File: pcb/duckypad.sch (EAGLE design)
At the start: 160 parts, among them IC2 REG1117, SW1 SPST_TACT-EVQQ2, SW2 SPST_TACT-EVQQ2, SW21 EC12E_SW, SW22 EC12E_SW, SW3 324_SW324_SWITCH_FOOT_HOLE, SW4 324_SW324_SWITCH_FOOT_HOLE, U1 USBC_16P, U2 USBC_16P, U3 ESP32-S3FN8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

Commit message: updated pcb files
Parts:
- removed JP3: (no value), adafruit_changed:PINHD-1X1CB
- removed U$3: BUZZ40402, duckypad:BUZZ40402
- added BZ1: BUZZ40402, duckypad:BUZZ40402
- added D22: 1N4148, duckypad:ADAFRUIT_CHANGED_DIODESOD-123
- added Q1: BSS123, transistor-small-signal:BSS123
- renumbered U$19 to U19
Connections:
- net +3V3: now also BZ1.PLUS, D22.C
- net GND: now also Q1.S, R19.1; no longer U$3.MINUS
- net N$37: now also BZ1.MINUS, D22.A, Q1.D; no longer R19.1, U$3.PLUS
- net N$70: now also Q1.G
- net N$73: no longer JP3.1
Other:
- note added: "BSS138"
- moved on the sheet: R19
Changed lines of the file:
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@@
 <drawing>
 <settings>
-<setting alwaysvectorfont="no"/>
+<setting alwaysvectorfont="yes"/>
 <setting keepoldvectorfont="yes"/>
 <setting verticaltext="up"/>
@@
 <part name="C28" library="clock" deviceset="CAP" device="0805" value="100nF"/>
 <part name="GND40" library="supply1" library_urn="urn:adsk.eagle:library:371" deviceset="GND" device=""/>
-<part name="U$19" library="SparkFun-Retired" deviceset="V_REG_TPS61040" device="SMD"/>
+<part name="U19" library="SparkFun-Retired" deviceset="V_REG_TPS61040" device="SMD"/>
 <part name="+3V32" library="supply1" library_urn="urn:adsk.eagle:library:371" deviceset="+3V3" device=""/>
 <part name="GND44" library="supply1" deviceset="GND" device=""/>
@@
 <part name="R17" library="joyAnalog" deviceset="RESISTOR" device="0805-RES" value="5K1"/>
 <part name="GND62" library="supply1" library_urn="urn:adsk.eagle:library:371" deviceset="GND" device=""/>
-<part name="JP3" library="adafruit_changed" deviceset="PINHD-1X1" device="CB"/>
 <part name="D1" library="duckypad" deviceset="ADAFRUIT_CHANGED_DIODE" device="SOD-123" value="1N4148"/>
 <part name="SW4" library="3pos_slide_switch" deviceset="324_SW" device="324_SWITCH_FOOT_HOLE" value="324_SW324_SWITCH_FOOT_HOLE"/>
@@
 <part name="GND65" library="supply1" deviceset="GND" device=""/>
 <part name="JP4" library="SparkFun-Jumpers" deviceset="JUMPER-SMT_2_NO" device="_NO-SILK"/>
-<part name="U$3" library="duckypad" deviceset="BUZZ40402" device=""/>
-<part name="R19" library="joyAnalog" deviceset="RESISTOR" device="0805-RES" value="5K1"/>
+<part name="BZ1" library="duckypad" deviceset="BUZZ40402" device=""/>
 <part name="GND41" library="supply1" deviceset="GND" device=""/>
+<part name="Q1" library="transistor-small-signal" library_urn="urn:adsk.eagle:library:401" deviceset="BSS123" device="" package3d_urn="urn:adsk.eagle:package:28738/2"/>
+<part name="+3V2" library="supply1" library_urn="urn:adsk.eagle:library:371" deviceset="+3V3" device=""/>
+<part name="D22" library="duckypad" deviceset="ADAFRUIT_CHANGED_DIODE" device="SOD-123" value="1N4148"/>
+<part name="R19" library="joyAnalog" deviceset="RESISTOR" device="0805-RES" value="5K1"/>
+<part name="GND67" library="supply1" deviceset="GND" device=""/>
 </parts>
 <sheets>
@@
 <plain>
 <text x="297.18" y="-63.5" size="1.778" layer="94">40MHz!!!</text>
+<text x="63.5" y="-264.16" size="1.778" layer="94">BSS138</text>
 </plain>
 <instances>
@@
 <attribute name="VALUE" x="505.46" y="-35.56" size="1.778" layer="96"/>
 </instance>
-<instance part="U$19" gate="G$1" x="190.5" y="-284.48" smashed="yes">
+<instance part="U19" gate="G$1" x="190.5" y="-284.48" smashed="yes">
 <attribute name="NAME" x="185.42" y="-274.32" size="1.778" layer="95" rot="MR180"/>
 <attribute name="VALUE" x="185.42" y="-294.64" size="1.778" layer="96"/>
@@
 <attribute name="VALUE" x="373.38" y="-297.18" size="1.778" layer="96"/>
 </instance>
-<instance part="JP3" gate="G$1" x="317.5" y="-71.12" smashed="yes" rot="R180">
-<attribute name="NAME" x="323.85" y="-74.295" size="1.778" layer="95" rot="R180"/>
-<attribute name="VALUE" x="323.85" y="-66.04" size="1.778" layer="96" rot="R180"/>
-</instance>
 <instance part="D1" gate="G$1" x="210.82" y="-251.46" smashed="yes">
 <attribute name="NAME" x="208.28" y="-248.92" size="1.27" layer="95"/>
@@
 <attribute name="NAME" x="340.36" y="-7.62" size="1.778" layer="95" font="vector" rot="R90"/>
 </instance>
-<instance part="U$3" gate="G$1" x="93.98" y="-220.98" smashed="yes" rot="MR0"/>
-<instance part="R19" gate="G$1" x="119.38" y="-220.98" smashed="yes" rot="MR180">
-<attribute name="NAME" x="118.11" y="-217.3986" size="1.778" layer="95" rot="MR180"/>
-<attribute name="VALUE" x="118.11" y="-215.138" size="1.778" layer="96" rot="MR180"/>
+<instance part="BZ1" gate="G$1" x="76.2" y="-228.6" smashed="yes" rot="MR270"/>
+<instance part="GND41" gate="1" x="76.2" y="-271.78" smashed="yes" rot="MR0">
+<attribute name="VALUE" x="78.74" y="-274.32" size="1.778" layer="96" rot="MR0"/>
+</instance>
+<instance part="Q1" gate="G$1" x="76.2" y="-256.54" smashed="yes" rot="MR0">
+<attribute name="NAME" x="73.66" y="-256.54" size="1.778" layer="95" rot="MR0"/>
+<attribute name="VALUE" x="73.66" y="-259.08" size="1.778" layer="96" rot="MR0"/>
+</instance>
+<instance part="+3V2" gate="G$1" x="76.2" y="-200.66" smashed="yes" rot="MR0">
+<attribute name="VALUE" x="78.74" y="-205.74" size="1.778" layer="96" rot="MR90"/>
+</instance>
+<instance part="D22" gate="G$1" x="60.96" y="-228.6" smashed="yes" rot="R90">
+<attribute name="NAME" x="58.42" y="-231.14" size="1.27" layer="95" rot="R90"/>
+<attribute name="VALUE" x="64.77" y="-231.14" size="1.27" layer="96" rot="R90"/>
+</instance>
+<instance part="R19" gate="G$1" x="91.44" y="-264.16" smashed="yes" rot="MR90">
+<attribute name="NAME" x="87.8586" y="-265.43" size="1.778" layer="95" rot="MR90"/>
+<attribute name="VALUE" x="85.598" y="-265.43" size="1.778" layer="96" rot="MR90"/>
 </instance>
-<instance part="GND41" gate="1" x="71.12" y="-223.52" smashed="yes" rot="MR0">
-<attribute name="VALUE" x="73.66" y="-226.06" size="1.778" layer="96" rot="MR0"/>
+<instance part="GND67" gate="1" x="91.44" y="-271.78" smashed="yes" rot="MR0">
+<attribute name="VALUE" x="93.98" y="-274.32" size="1.778" layer="96" rot="MR0"/>
 </instance>
 </instances>
@@
 </segment>
 <segment>
-<pinref part="U$19" gate="G$1" pin="GND"/>
+<pinref part="U19" gate="G$1" pin="GND"/>
 <pinref part="GND45" gate="1" pin="GND"/>
 <wire x1="203.2" y1="-284.48" x2="205.74" y2="-284.48" width="0.1524" layer="91"/>
@@
 </segment>
 <segment>
+<pinref part="Q1" gate="G$1" pin="S"/>
 <pinref part="GND41" gate="1" pin="GND"/>
-<pinref part="U$3" gate="G$1" pin="MINUS"/>
-<wire x1="71.12" y1="-220.98" x2="78.74" y2="-220.98" width="0.1524" layer="91"/>
+<wire x1="76.2" y1="-269.24" x2="76.2" y2="-261.62" width="0.1524" layer="91"/>
+</segment>
+<segment>
+<pinref part="R19" gate="G$1" pin="1"/>
+<pinref part="GND67" gate="1" pin="GND"/>
 </segment>
 </net>
@@
 <wire x1="160.02" y1="-266.7" x2="172.72" y2="-266.7" width="0.1524" layer="91"/>
 <junction x="160.02" y="-266.7"/>
-<pinref part="U$19" gate="G$1" pin="VIN"/>
+<pinref part="U19" gate="G$1" pin="VIN"/>
 <wire x1="172.72" y1="-266.7" x2="182.88" y2="-266.7" width="0.1524" layer="91"/>
 <wire x1="180.34" y1="-279.4" x2="172.72" y2="-279.4" width="0.1524" layer="91"/>
 <wire x1="172.72" y1="-279.4" x2="172.72" y2="-266.7" width="0.1524" layer="91"/>
 <junction x="172.72" y="-266.7"/>
-<pinref part="U$19" gate="G$1" pin="EN"/>
+<pinref part="U19" gate="G$1" pin="EN"/>
 <wire x1="180.34" y1="-289.56" x2="172.72" y2="-289.56" width="0.1524" layer="91"/>
 <wire x1="172.72" y1="-289.56" x2="172.72" y2="-279.4" width="0.1524" layer="91"/>
@@
 <wire x1="147.32" y1="-208.28" x2="124.46" y2="-208.28" width="0.1524" layer="91"/>
 </segment>
+<segment>
+<pinref part="+3V2" gate="G$1" pin="+3V3"/>
+<pinref part="BZ1" gate="G$1" pin="PLUS"/>
+<wire x1="76.2" y1="-203.2" x2="76.2" y2="-213.36" width="0.1524" layer="91"/>
+<wire x1="76.2" y1="-213.36" x2="60.96" y2="-213.36" width="0.1524" layer="91"/>
+<wire x1="60.96" y1="-213.36" x2="60.96" y2="-226.06" width="0.1524" layer="91"/>
+<junction x="76.2" y="-213.36"/>
+<pinref part="D22" gate="G$1" pin="C"/>
+</segment>
 </net>
 <net name="USB_DP" class="0">
@@
 <segment>
 <wire x1="195.58" y1="-266.7" x2="205.74" y2="-266.7" width="0.1524" layer="91"/>
-<pinref part="U$19" gate="G$1" pin="SW"/>
+<pinref part="U19" gate="G$1" pin="SW"/>
 <wire x1="203.2" y1="-279.4" x2="205.74" y2="-279.4" width="0.1524" layer="91"/>
 <wire x1="205.74" y1="-279.4" x2="205.74" y2="-266.7" width="0.1524" layer="91"/>
@@
 <net name="N$39" class="0">
 <segment>
-<pinref part="U$19" gate="G$1" pin="FB"/>
+<pinref part="U19" gate="G$1" pin="FB"/>
 <wire x1="203.2" y1="-289.56" x2="208.28" y2="-289.56" width="0.1524" layer="91"/>
 <wire x1="208.28" y1="-289.56" x2="208.28" y2="-284.48" width="0.1524" layer="91"/>
@@
 <wire x1="373.38" y1="-220.98" x2="124.46" y2="-220.98" width="0.1524" layer="91"/>
 <pinref part="SH1" gate="G$1" pin="8"/>
-<pinref part="R19" gate="G$1" pin="2"/>
+<pinref part="Q1" gate="G$1" pin="G"/>
+<wire x1="81.28" y1="-259.08" x2="91.44" y2="-259.08" width="0.1524" layer="91"/>
+<wire x1="91.44" y1="-259.08" x2="99.06" y2="-259.08" width="0.1524" layer="91"/>
+<wire x1="124.46" y1="-220.98" x2="99.06" y2="-220.98" width="0.1524" layer="91"/>
+<wire x1="99.06" y1="-220.98" x2="99.06" y2="-259.08" width="0.1524" layer="91"/>
 <junction x="124.46" y="-220.98"/>
+<pinref part="R19" gate="G$1" pin="2"/>
+<junction x="91.44" y="-259.08"/>
 </segment>
 </net>
@@
 <wire x1="347.98" y1="-71.12" x2="335.28" y2="-71.12" width="0.1524" layer="91"/>
 <wire x1="335.28" y1="-71.12" x2="335.28" y2="-226.06" width="0.1524" layer="91"/>
-<pinref part="JP3" gate="G$1" pin="1"/>
-<wire x1="335.28" y1="-71.12" x2="320.04" y2="-71.12" width="0.1524" layer="91"/>
-<junction x="335.28" y="-71.12"/>
 <wire x1="335.28" y1="-226.06" x2="124.46" y2="-226.06" width="0.1524" layer="91"/>
 <pinref part="SH1" gate="G$1" pin="10"/>
@@
 <net name="N$37" class="0">
 <segment>
-<pinref part="U$3" gate="G$1" pin="PLUS"/>
-<pinref part="R19" gate="G$1" pin="1"/>
-<wire x1="109.22" y1="-220.98" x2="114.3" y2="-220.98" width="0.1524" layer="91"/>
+<pinref part="BZ1" gate="G$1" pin="MINUS"/>
+<pinref part="Q1" gate="G$1" pin="D"/>
+<wire x1="76.2" y1="-243.84" x2="76.2" y2="-251.46" width="0.1524" layer="91"/>
+<wire x1="76.2" y1="-243.84" x2="60.96" y2="-243.84" width="0.1524" layer="91"/>
+<wire x1="60.96" y1="-243.84" x2="60.96" y2="-231.14" width="0.1524" layer="91"/>
+<junction x="76.2" y="-243.84"/>
+<pinref part="D22" gate="G$1" pin="A"/>
 </segment>
 </net>

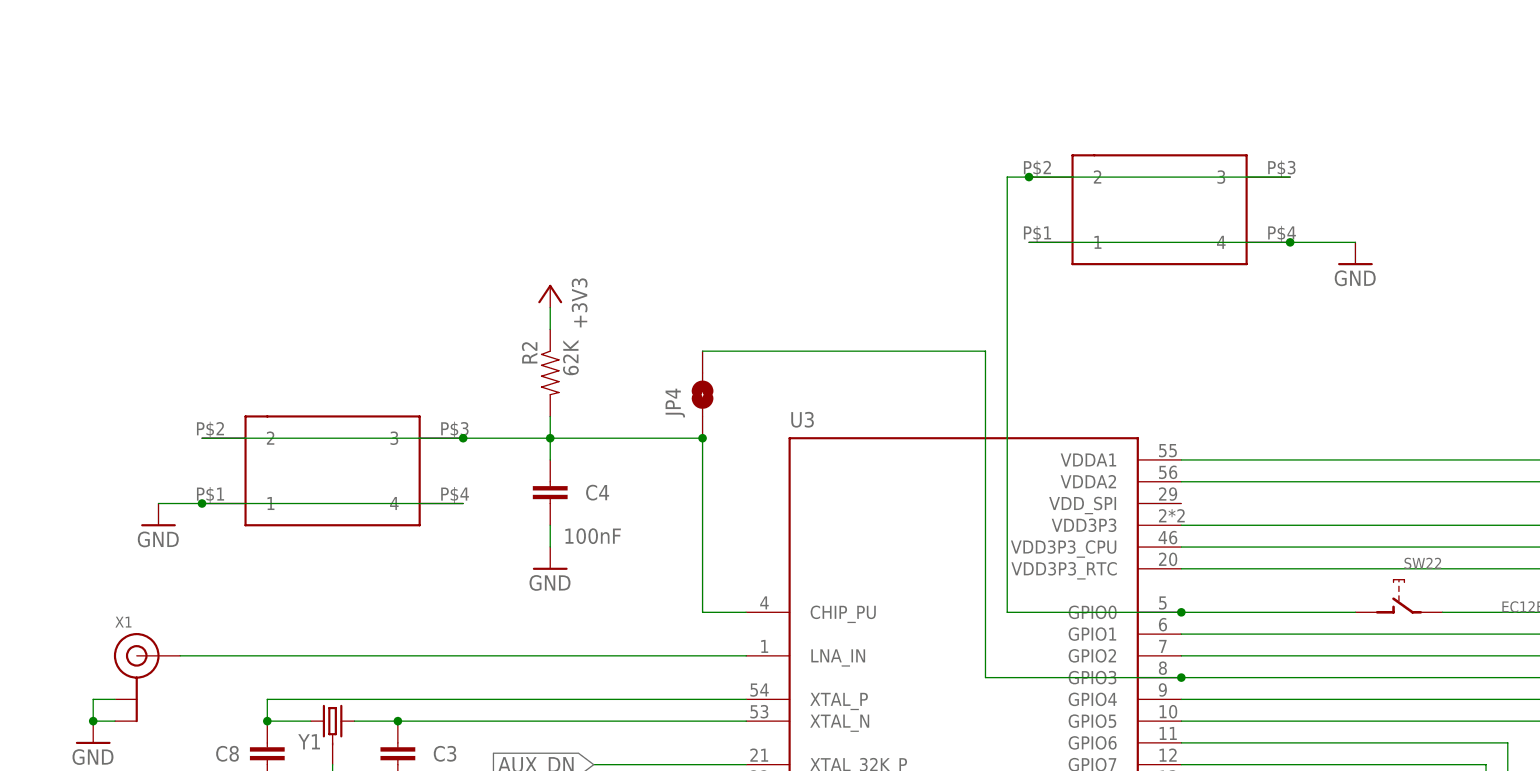
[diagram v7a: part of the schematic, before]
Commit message: new side push button
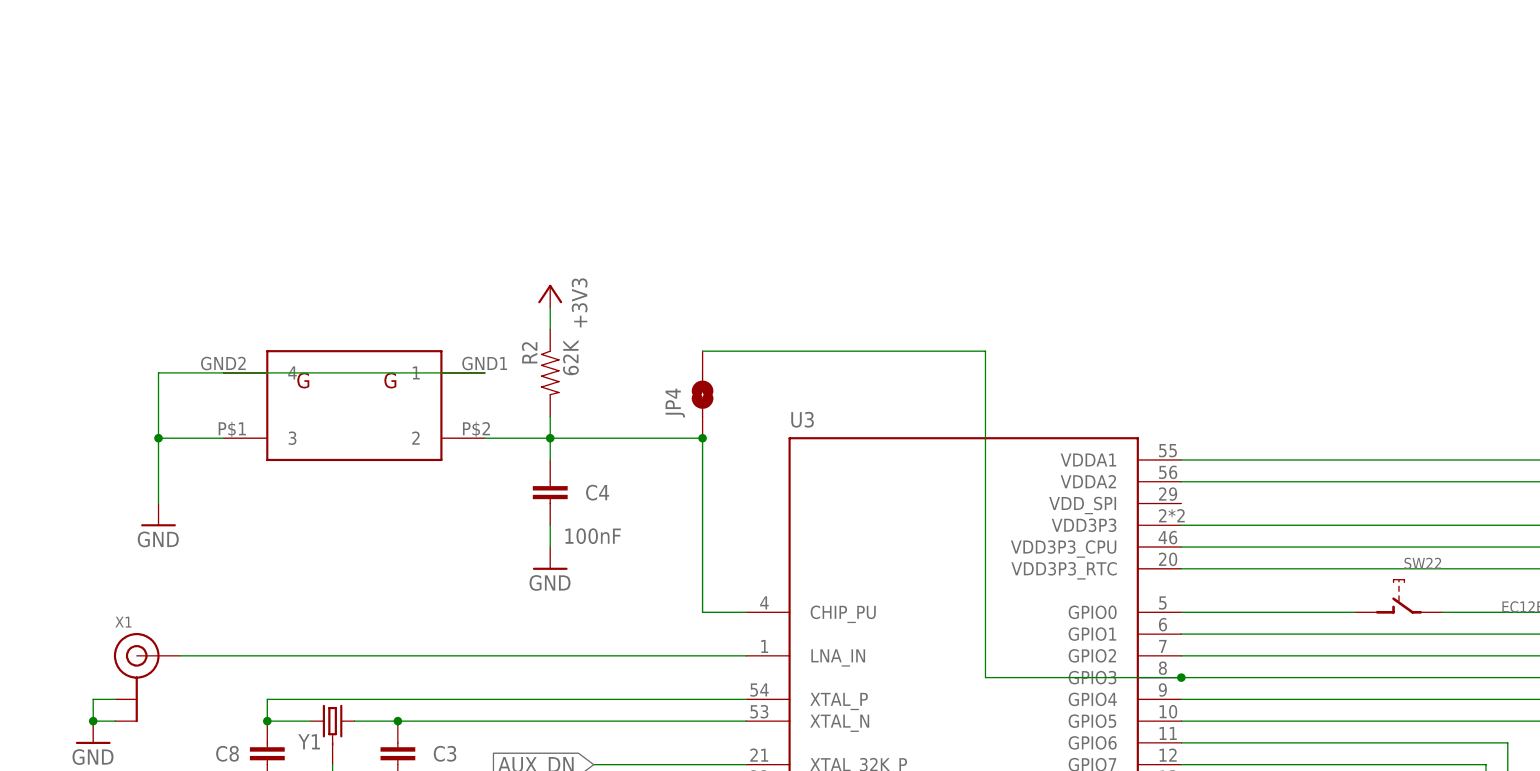
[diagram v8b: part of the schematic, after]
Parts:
- removed SW4: 324_SW324_SWITCH_FOOT_HOLE, 3pos_slide_switch:324_SW324_SWITCH_FOOT_HOLE
- SW3: value 324_SW324_SWITCH_FOOT_HOLE -> 3POS_SLIDE_SWITCH_324_SW; device 3pos_slide_switch:324_SW324_SWITCH_FOOT_HOLE -> duckypad:3POS_SLIDE_SWITCH_324_SW
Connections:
- net GND: now also SW3.3; no longer SW4.1, SW4.4
- net N$28: no longer SW4.2, SW4.3
- net RESET: no longer SW3.3
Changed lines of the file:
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@@
 <part name="C4" library="clock" deviceset="CAP" device="0805" value="100nF"/>
 <part name="GND32" library="clock" deviceset="GND" device=""/>
-<part name="SW3" library="3pos_slide_switch" deviceset="324_SW" device="324_SWITCH_FOOT_HOLE" value="324_SW324_SWITCH_FOOT_HOLE"/>
+<part name="SW3" library="duckypad" deviceset="3POS_SLIDE_SWITCH_324_SW" device="" value="3POS_SLIDE_SWITCH_324_SW"/>
 <part name="GND33" library="clock" deviceset="GND" device=""/>
 <part name="GND34" library="clock" deviceset="GND" device=""/>
@@
 <part name="GND62" library="supply1" library_urn="urn:adsk.eagle:library:371" deviceset="GND" device=""/>
 <part name="D1" library="duckypad" deviceset="ADAFRUIT_CHANGED_DIODE" device="SOD-123" value="1N4148"/>
-<part name="SW4" library="3pos_slide_switch" deviceset="324_SW" device="324_SWITCH_FOOT_HOLE" value="324_SW324_SWITCH_FOOT_HOLE"/>
 <part name="D2" library="duckypad" deviceset="ADAFRUIT_CHANGED_DIODE" device="SOD-123" value="1N4148"/>
 <part name="D3" library="duckypad" deviceset="ADAFRUIT_CHANGED_DIODE" device="SOD-123" value="1N4148"/>
@@
 <part name="D21" library="duckypad" deviceset="ADAFRUIT_CHANGED_DIODE" device="SOD-123" value="1N4148"/>
 <part name="GND1" library="supply1" library_urn="urn:adsk.eagle:library:371" deviceset="GND" device=""/>
-<part name="GND54" library="clock" deviceset="GND" device=""/>
 <part name="GND61" library="supply1" library_urn="urn:adsk.eagle:library:371" deviceset="GND" device=""/>
 <part name="GND63" library="supply1" library_urn="urn:adsk.eagle:library:371" deviceset="GND" device=""/>
@@
 <attribute name="VALUE" x="322.58" y="-27.94" size="1.778" layer="96"/>
 </instance>
-<instance part="SW3" gate="G$1" x="299.72" y="-15.24" smashed="yes"/>
+<instance part="SW3" gate="G$1" x="302.26" y="-5.08" smashed="yes" rot="R180"/>
 <instance part="GND33" gate="1" x="279.4" y="-20.32" smashed="yes">
 <attribute name="VALUE" x="276.86" y="-22.86" size="1.778" layer="96"/>
@@
 <attribute name="VALUE" x="208.28" y="-255.27" size="1.27" layer="96"/>
 </instance>
-<instance part="SW4" gate="G$1" x="396.24" y="15.24" smashed="yes"/>
 <instance part="D2" gate="G$1" x="2.54" y="25.4" smashed="yes" rot="R270">
 <attribute name="NAME" x="5.08" y="27.94" size="1.27" layer="95" rot="R270"/>
@@
 <instance part="GND1" gate="1" x="330.2" y="-269.24" smashed="yes">
 <attribute name="VALUE" x="327.66" y="-271.78" size="1.778" layer="96"/>
-</instance>
-<instance part="GND54" gate="1" x="419.1" y="10.16" smashed="yes">
-<attribute name="VALUE" x="416.56" y="7.62" size="1.778" layer="96"/>
 </instance>
 <instance part="GND61" gate="1" x="474.98" y="-149.86" smashed="yes">
@@
 </segment>
 <segment>
-<pinref part="GND33" gate="1" pin="GND"/>
-<pinref part="SW3" gate="G$1" pin="1"/>
-<wire x1="279.4" y1="-17.78" x2="284.48" y2="-17.78" width="0.1524" layer="91"/>
-<pinref part="SW3" gate="G$1" pin="4"/>
-<wire x1="284.48" y1="-17.78" x2="314.96" y2="-17.78" width="0.1524" layer="91"/>
-<junction x="284.48" y="-17.78"/>
-</segment>
-<segment>
 <pinref part="X1" gate="G$1" pin="GND@1"/>
 <pinref part="GND34" gate="1" pin="GND"/>
@@
 </segment>
 <segment>
-<pinref part="GND54" gate="1" pin="GND"/>
-<pinref part="SW4" gate="G$1" pin="4"/>
-<wire x1="419.1" y1="12.7" x2="411.48" y2="12.7" width="0.1524" layer="91"/>
-<pinref part="SW4" gate="G$1" pin="1"/>
-<wire x1="411.48" y1="12.7" x2="381" y2="12.7" width="0.1524" layer="91"/>
-<junction x="411.48" y="12.7"/>
-</segment>
-<segment>
 <pinref part="SW1" gate="G$1" pin="P"/>
 <pinref part="SW1" gate="G$1" pin="P1"/>
@@
 <pinref part="R19" gate="G$1" pin="1"/>
 <pinref part="GND67" gate="1" pin="GND"/>
+</segment>
+<segment>
+<pinref part="GND33" gate="1" pin="GND"/>
+<wire x1="279.4" y1="-17.78" x2="279.4" y2="-10.16" width="0.1524" layer="91"/>
+<pinref part="SW3" gate="G$1" pin="3"/>
+<wire x1="279.4" y1="-10.16" x2="287.02" y2="-10.16" width="0.1524" layer="91"/>
+<pinref part="SW3" gate="G$1" pin="4"/>
+<wire x1="279.4" y1="-10.16" x2="279.4" y2="-2.54" width="0.1524" layer="91"/>
+<wire x1="279.4" y1="-2.54" x2="287.02" y2="-2.54" width="0.1524" layer="91"/>
+<junction x="279.4" y="-10.16"/>
+<pinref part="SW3" gate="G$1" pin="1"/>
+<wire x1="317.5" y1="-2.54" x2="287.02" y2="-2.54" width="0.1524" layer="91"/>
 </segment>
 </net>
@@
 <net name="RESET" class="0">
 <segment>
-<pinref part="SW3" gate="G$1" pin="2"/>
-<pinref part="SW3" gate="G$1" pin="3"/>
-<wire x1="284.48" y1="-10.16" x2="314.96" y2="-10.16" width="0.1524" layer="91"/>
 <pinref part="R2" gate="G$1" pin="2"/>
 <pinref part="C4" gate="G$1" pin="1"/>
@@
 <wire x1="342.9" y1="-10.16" x2="325.12" y2="-10.16" width="0.1524" layer="91"/>
 <junction x="325.12" y="-10.16"/>
-<wire x1="314.96" y1="-10.16" x2="325.12" y2="-10.16" width="0.1524" layer="91"/>
-<junction x="314.96" y="-10.16"/>
 <pinref part="JP4" gate="G$1" pin="1"/>
 <junction x="342.9" y="-10.16"/>
+<pinref part="SW3" gate="G$1" pin="2"/>
+<wire x1="317.5" y1="-10.16" x2="325.12" y2="-10.16" width="0.1524" layer="91"/>
 </segment>
 </net>
@@
 <net name="N$28" class="0">
 <segment>
-<pinref part="SW4" gate="G$1" pin="3"/>
-<pinref part="SW4" gate="G$1" pin="2"/>
-<wire x1="411.48" y1="20.32" x2="381" y2="20.32" width="0.1524" layer="91"/>
-<wire x1="381" y1="20.32" x2="378.46" y2="20.32" width="0.1524" layer="91"/>
-<junction x="381" y="20.32"/>
 <pinref part="U3" gate="G$1" pin="GPIO0"/>
 <pinref part="SW22" gate="G$2" pin="1"/>
 <wire x1="398.78" y1="-30.48" x2="419.1" y2="-30.48" width="0.1524" layer="91"/>
-<wire x1="378.46" y1="20.32" x2="378.46" y2="-30.48" width="0.1524" layer="91"/>
-<wire x1="378.46" y1="-30.48" x2="398.78" y2="-30.48" width="0.1524" layer="91"/>
-<junction x="398.78" y="-30.48"/>
-</segment>
-</net>
+</segment>
+</net>
